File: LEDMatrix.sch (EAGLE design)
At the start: 22 parts

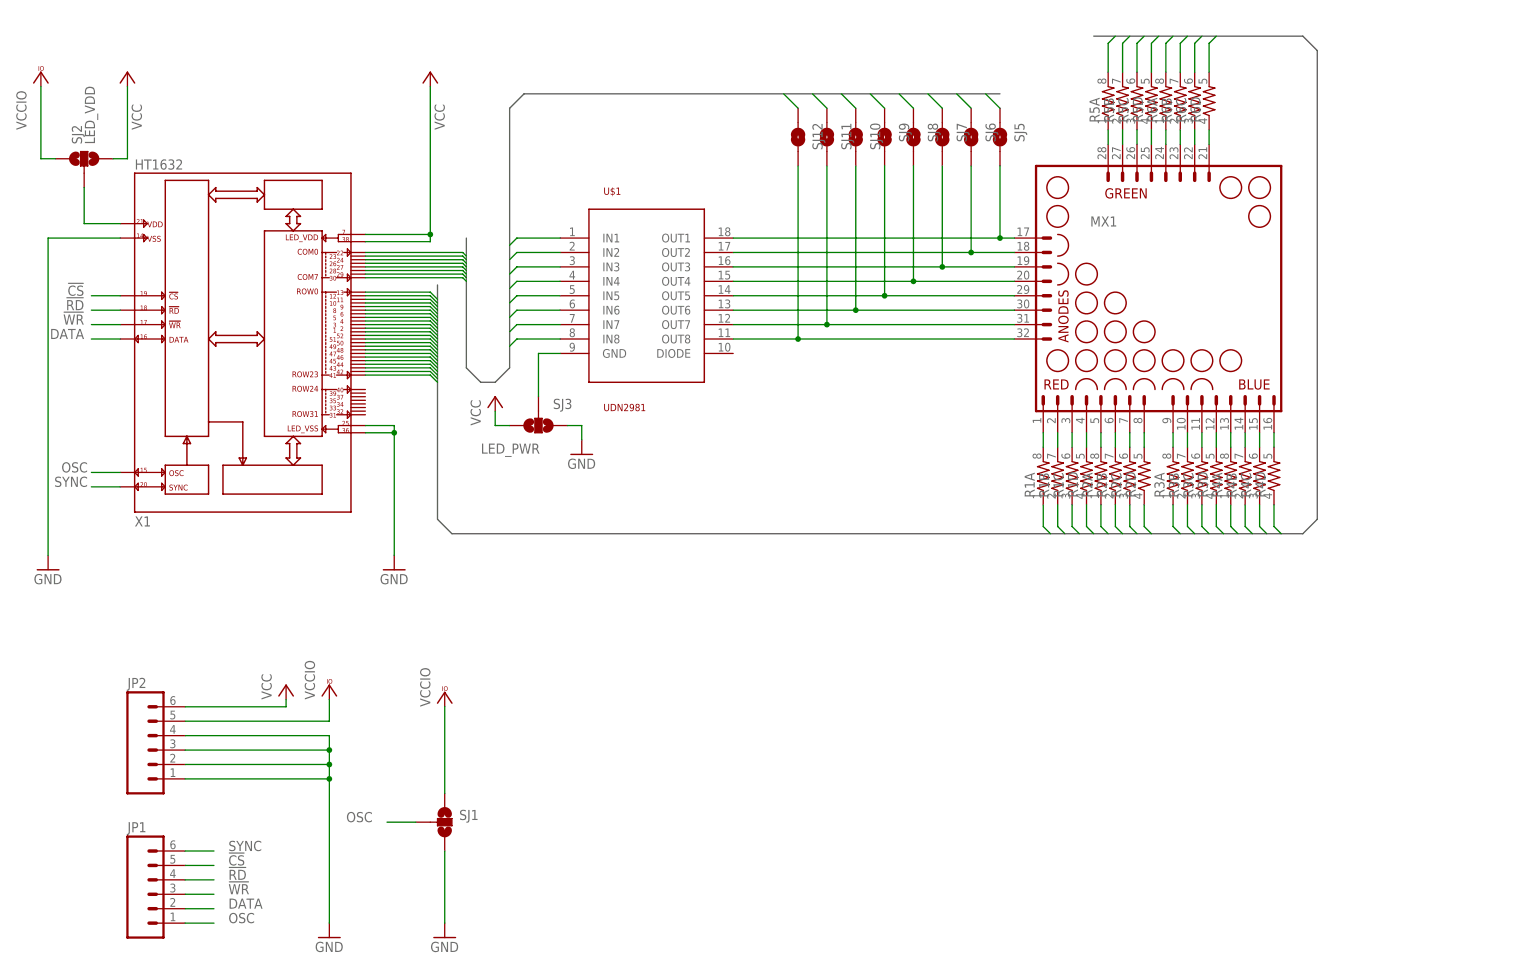
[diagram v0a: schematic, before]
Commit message: updated silk layer
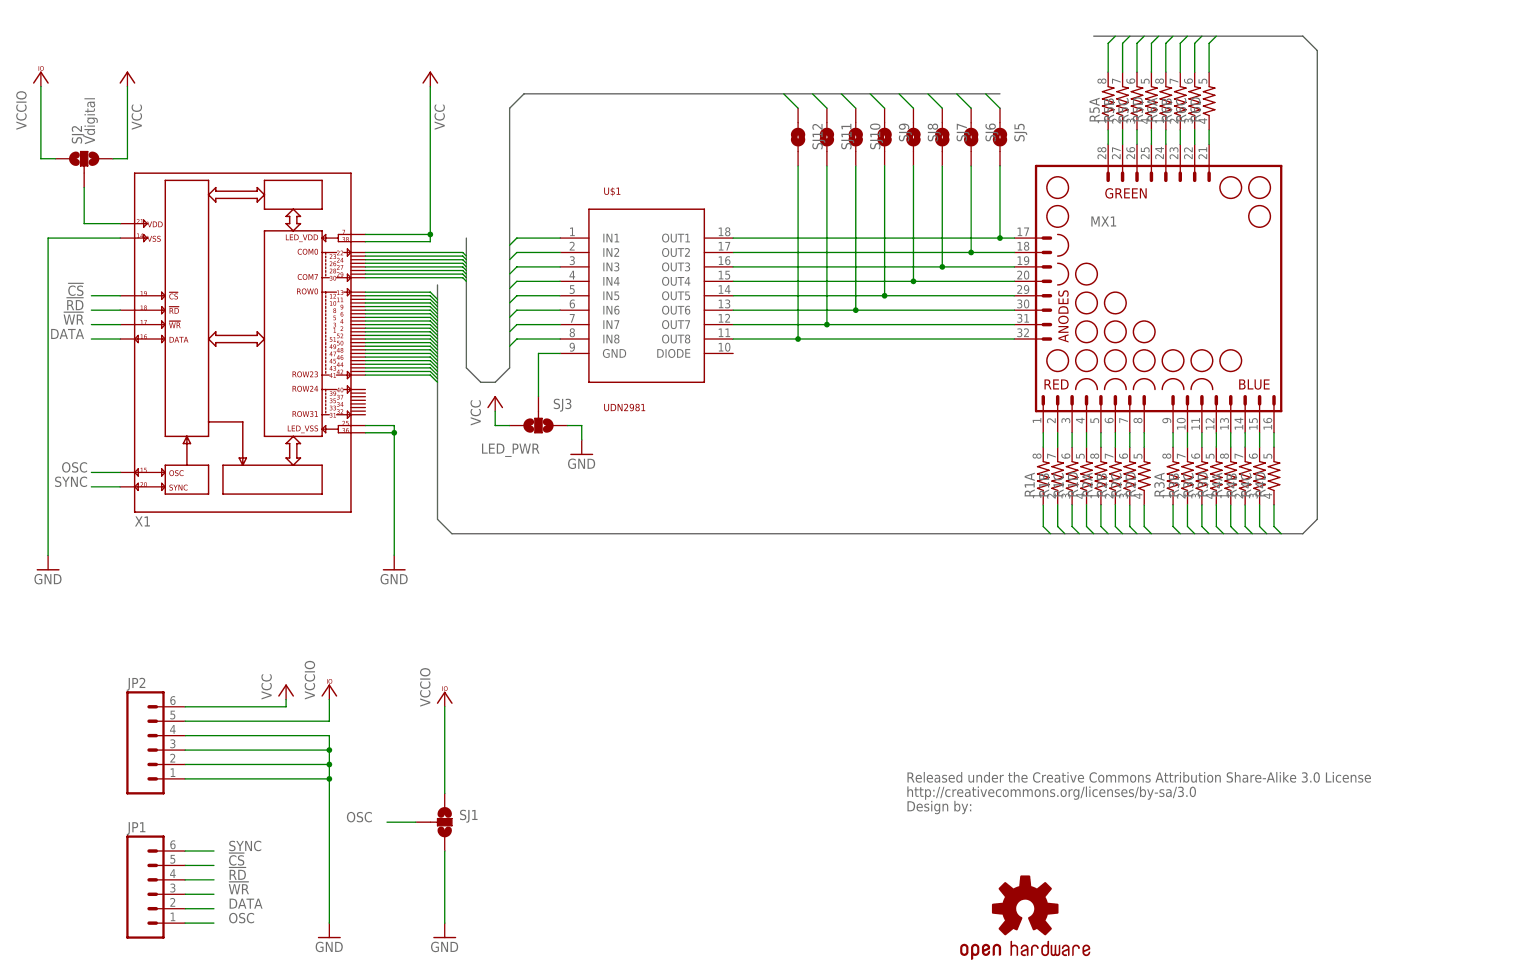
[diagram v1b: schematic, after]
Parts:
- added CC_TEXT1: CREATIVE_COMMONS, SparkFun-Aesthetics:CREATIVE_COMMONS
- added LOGO1: OSHW-LOGOL, SparkFun-Aesthetics:OSHW-LOGOL
- SJ2: value LED_VDD -> Vdigital
- X1: device HT1632:HT1632CV120 -> siebecke:HT1632C12

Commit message: replaced parts library (schematic only)
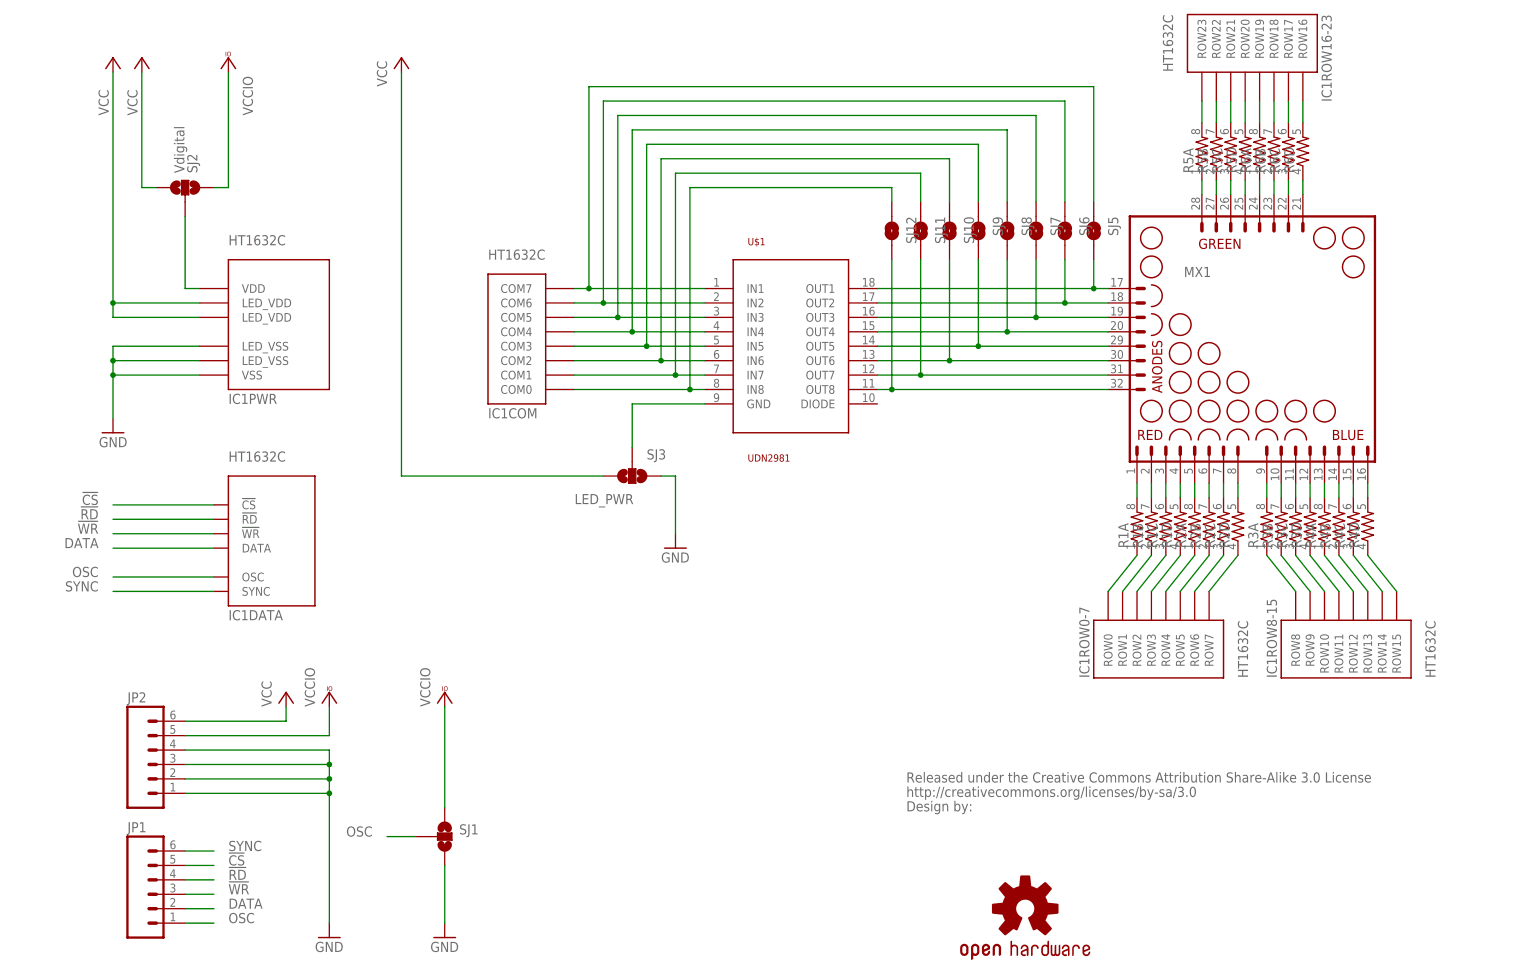
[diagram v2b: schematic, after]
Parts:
- removed X1: (no value), siebecke:HT1632C12
- added IC1: HT1632C, ht1632:HT1632
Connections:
- net !CS: now also IC1DATA.!CS; no longer X1.!CS
- net !RD: now also IC1DATA.!RD; no longer X1.!RD
- net !WR: now also IC1DATA.!WR; no longer X1.!WR
- net COM0: now also IC1COM.COM0; no longer X1.COM0
- net COM1: now also IC1COM.COM1; no longer X1.COM1
- net COM2: now also IC1COM.COM2; no longer X1.COM2
- net COM3: now also IC1COM.COM3; no longer X1.COM3
- net COM4: now also IC1COM.COM4; no longer X1.COM4
- net COM5: now also IC1COM.COM5; no longer X1.COM5
- net COM6: now also IC1COM.COM6; no longer X1.COM6
- net COM7: now also IC1COM.COM7; no longer X1.COM7
- net DATA: now also IC1DATA.DATA; no longer X1.DATA
- net GND: now also IC1PWR.LED_VSS@1, IC1PWR.LED_VSS@2, IC1PWR.VSS; no longer X1.LED_VSS1, X1.LED_VSS2, X1.VSS
- net N$9: now also IC1PWR.VDD; no longer X1.VDD
- net OSC: now also IC1DATA.OSC; no longer X1.OSC
- net ROW0: now also IC1ROW0-7.ROW0; no longer X1.ROW0
- net ROW1: now also IC1ROW0-7.ROW1; no longer X1.ROW1
- net ROW10: now also IC1ROW8-15.ROW10; no longer X1.ROW10
- net ROW11: now also IC1ROW8-15.ROW11; no longer X1.ROW11
- net ROW12: now also IC1ROW8-15.ROW12; no longer X1.ROW12
- net ROW13: now also IC1ROW8-15.ROW13; no longer X1.ROW13
- net ROW14: now also IC1ROW8-15.ROW14; no longer X1.ROW14
- net ROW15: now also IC1ROW8-15.ROW15; no longer X1.ROW15
- net ROW16: now also IC1ROW16-23.ROW16; no longer X1.ROW16
- net ROW17: now also IC1ROW16-23.ROW17; no longer X1.ROW17
- net ROW18: now also IC1ROW16-23.ROW18; no longer X1.ROW18
- net ROW19: now also IC1ROW16-23.ROW19; no longer X1.ROW19
- net ROW2: now also IC1ROW0-7.ROW2; no longer X1.ROW2
- net ROW20: now also IC1ROW16-23.ROW20; no longer X1.ROW20
- net ROW21: now also IC1ROW16-23.ROW21; no longer X1.ROW21
- net ROW22: now also IC1ROW16-23.ROW22; no longer X1.ROW22
- net ROW23: now also IC1ROW16-23.ROW23; no longer X1.ROW23
- net ROW3: now also IC1ROW0-7.ROW3; no longer X1.ROW3
- net ROW4: now also IC1ROW0-7.ROW4; no longer X1.ROW4
- net ROW5: now also IC1ROW0-7.ROW5; no longer X1.ROW5
- net ROW6: now also IC1ROW0-7.ROW6; no longer X1.ROW6
- net ROW7: now also IC1ROW0-7.ROW7; no longer X1.ROW7
- net ROW8: now also IC1ROW8-15.ROW8; no longer X1.ROW8
- net ROW9: now also IC1ROW8-15.ROW9; no longer X1.ROW9
- net SYNC: now also IC1DATA.SYNC; no longer X1.SYNC
- net VCC: now also IC1PWR.LED_VDD@1, IC1PWR.LED_VDD@2; no longer X1.LED_VDD1, X1.LED_VDD2
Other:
- moved on the sheet: JP2, MX1, R1A, R1B, R1C, R1D, R2A, R2B, R2C, R2D, R3A, R3B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
